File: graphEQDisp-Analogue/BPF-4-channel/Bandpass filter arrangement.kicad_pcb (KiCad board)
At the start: 2 copper layers, 73 parts, among them J2 pick-up_level_pot, J3 PWR, J4 Raw_Sig, Q1 Q_NPN_EBC, U1 LM358, U2 LM358, U3 LM358, U4 LM386, U5 LM358, U6 LM358, U7 LM358

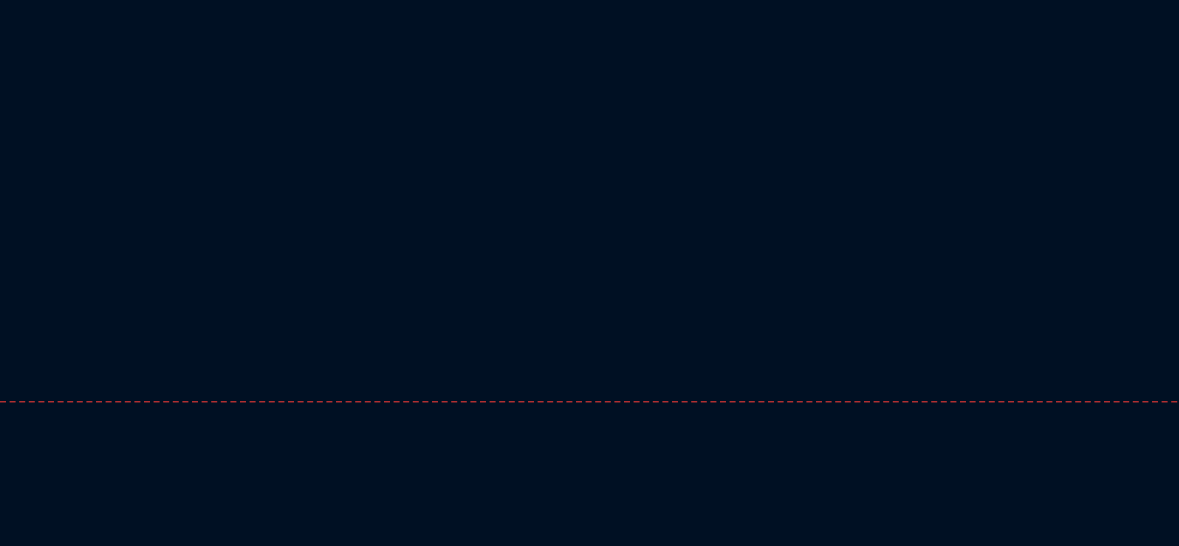
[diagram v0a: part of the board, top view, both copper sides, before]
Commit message: Added note to graphics equliser display PCB
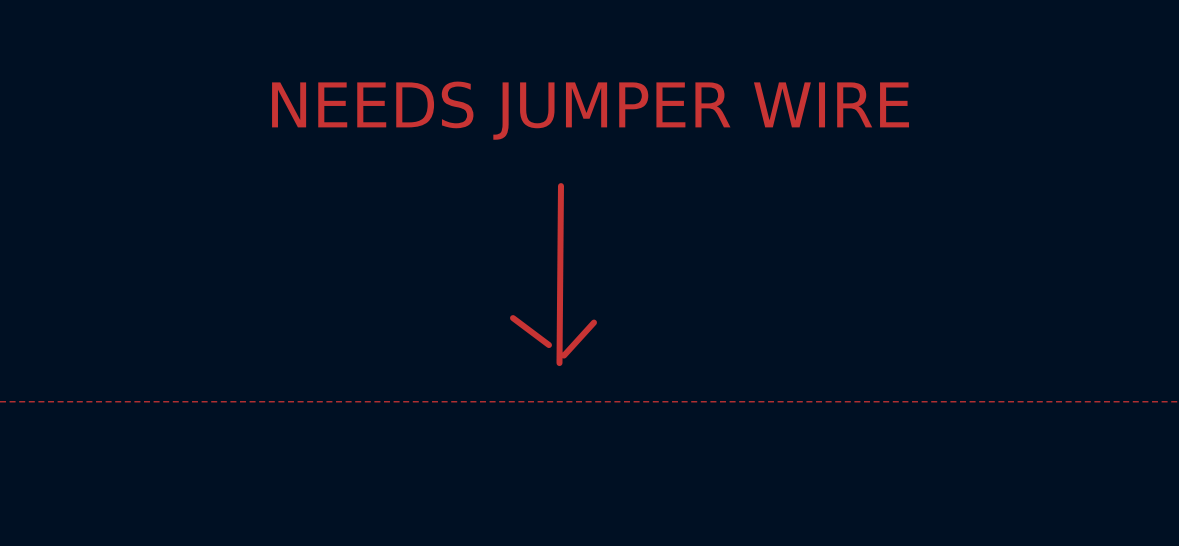
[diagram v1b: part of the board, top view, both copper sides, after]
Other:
- board text added: "NEEDS JUMPER WIRE"
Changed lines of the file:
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@@
     )
   )
+  (gr_line (start 149.45 26.65) (end 149.5 20.75) (layer "F.Cu") (width 0.2))
+  (gr_line (start 149.1 26.05) (end 147.9 25.15) (layer "F.Cu") (width 0.2))
+  (gr_line (start 149.6 26.4) (end 150.6 25.3) (layer "F.Cu") (width 0.2))
   (gr_text "KAPZ_&_PON_ELECTRIX- -GRAPHICS EQUALISER DISPLAY" (at 98.806 30.48) (layer "F.Cu")
     (effects (font (size 1.5 1.5) (thickness 0.3)))
   )
+  (gr_text "NEEDS JUMPER WIRE\n" (at 150.45 18.1) (layer "F.Cu")
+    (effects (font (size 1.5 1.5) (thickness 0.3)))
+  )
